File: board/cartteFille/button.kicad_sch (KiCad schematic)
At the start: 13 parts, among them U21-2 SN74LVC2G14DBVTG4

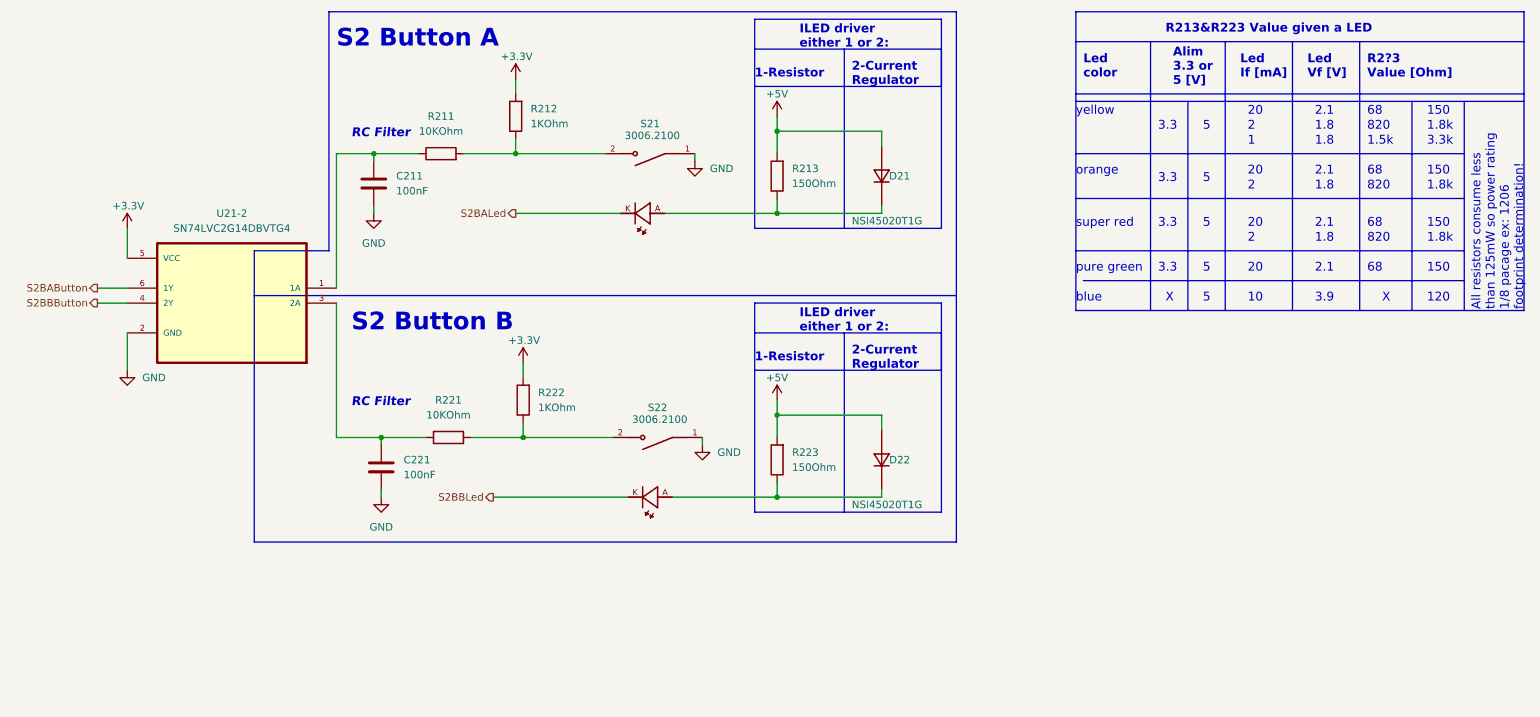
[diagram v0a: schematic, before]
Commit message: improve schematic
+ replace AOP with a jellybean one (LM358)
+ better usage of master board pins
+ graphical improvements
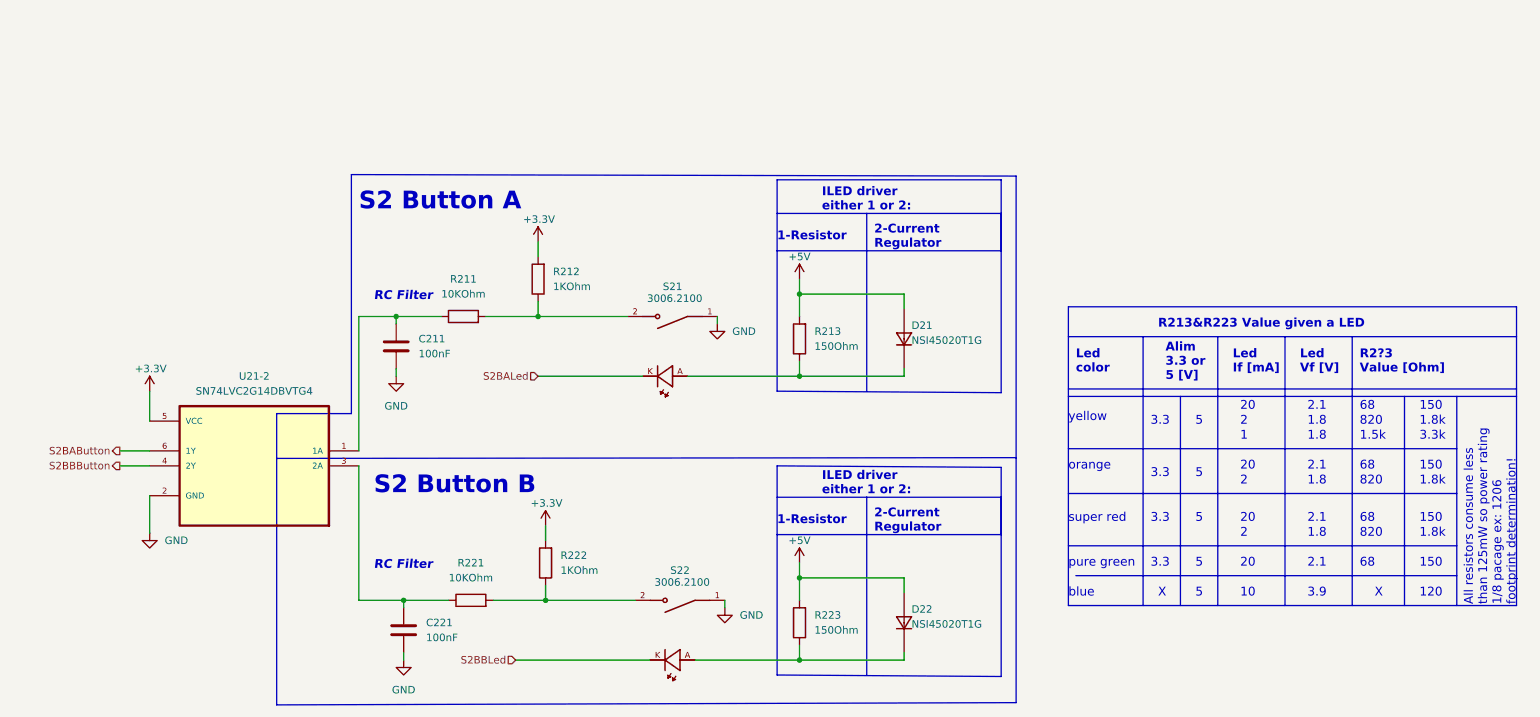
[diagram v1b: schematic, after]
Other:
- moved on the sheet: C211, C221, D21, D22, R211, R212, R213, R221, R222, R223, S21, S22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
